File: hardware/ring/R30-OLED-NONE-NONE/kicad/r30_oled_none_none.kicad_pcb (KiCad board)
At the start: 2 copper layers, 43 x 18 mm, 32 parts, among them J1 USB4215-class 16P TH stakes, Q1 SI2301 P-FET, Q2 2N7002 gate driver, SW1 5mm 200gf dome, U1 ESP32-C3-MINI-1-N4, U2 PAW3204DB-TJ3L, U3 TP4054, U4 RT9080-33GJ5

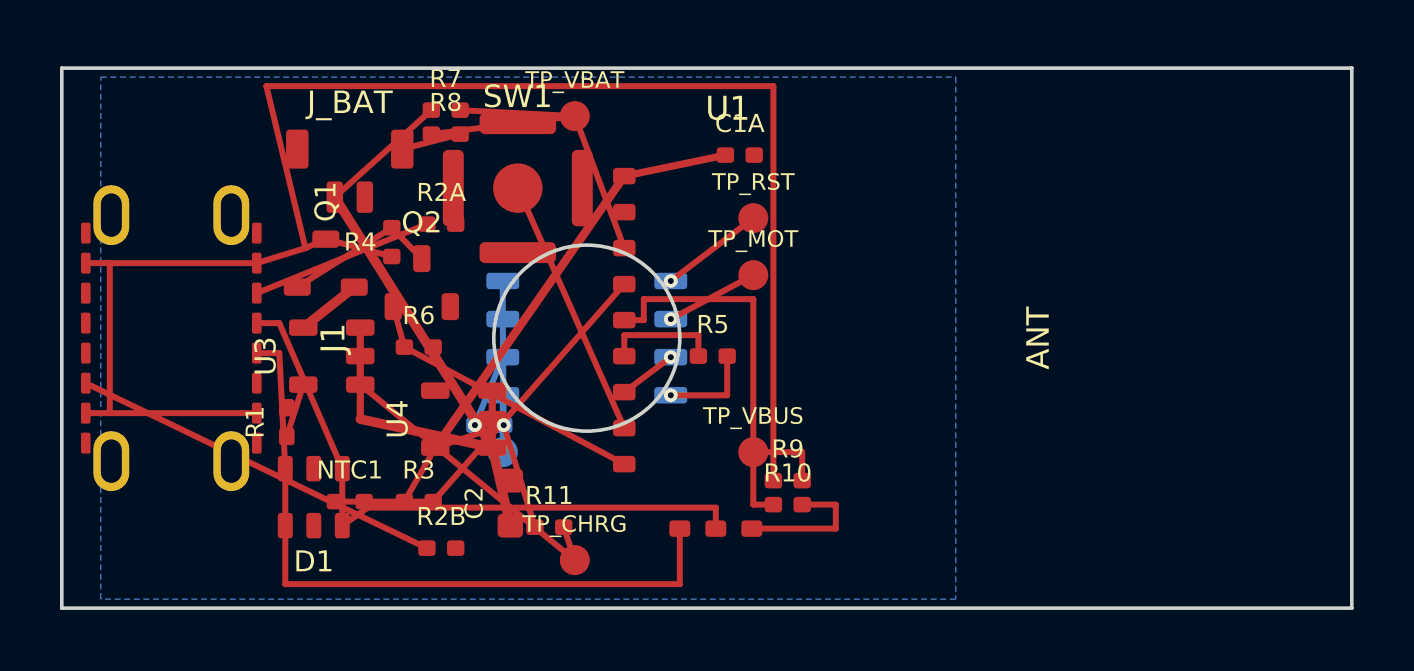
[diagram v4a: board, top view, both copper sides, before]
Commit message: fix(r30): clear connector cluster routing debt
Sensing mechanism: PAW3204 optical surface tracking.

Form factor and angle: R30 30-degree ring, OLED/NONE/NONE active lane; connector-side CC2 and thermistor divider routing cleanup.

Intended use: accessibility-first BLE HID pointing first-board validation.

BOM estimate: active R30 prototype remains about .30-.45, target about ; routing and placement-only change adds no BOM line.
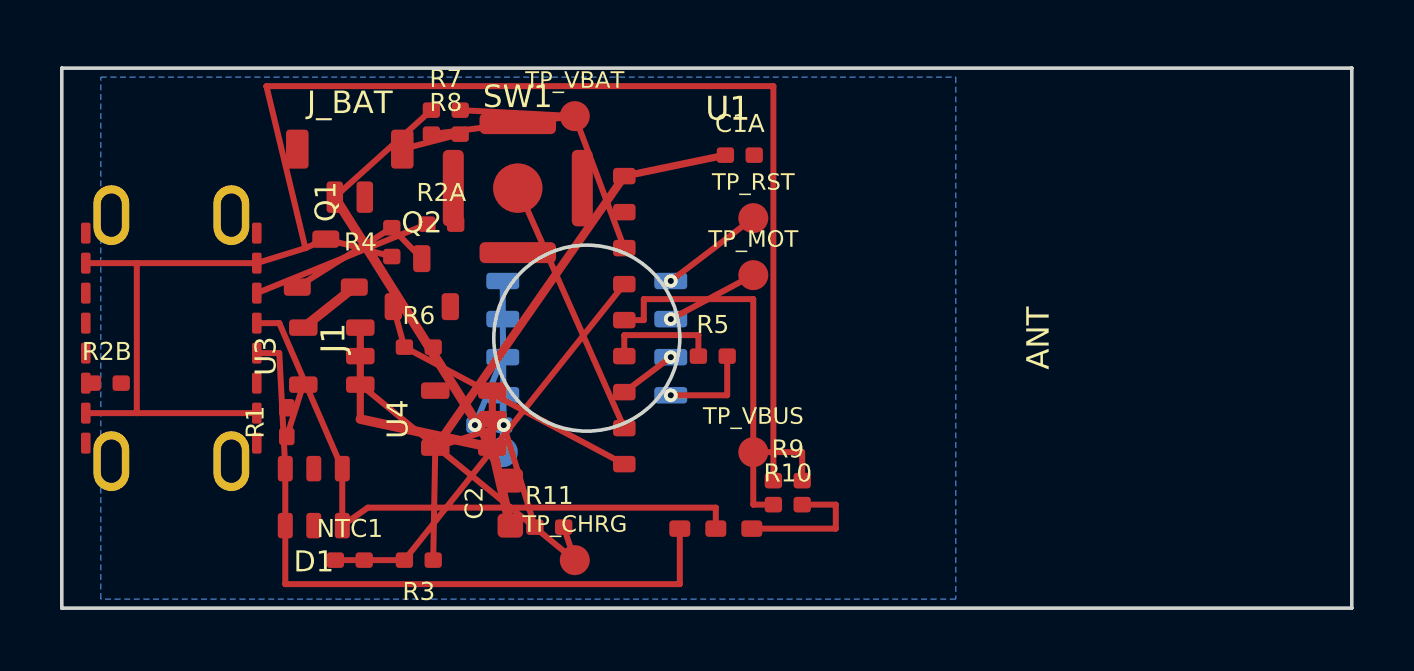
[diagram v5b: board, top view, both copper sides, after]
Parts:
- moved R2B 12.4 mm to (100.5, 101.5)
- moved NTC1 1.95 mm to (108.6, 107.4)
- moved R3 1.95 mm to (110.9, 107.4), turned to 180 degrees
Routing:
- net USB_CC2_RD: track 12.6 -> 0.22 mm
- net VREG_3V3: track 27.3 -> 29.0 mm
- net NTC_SENSE: track 12.9 -> 14.1 mm
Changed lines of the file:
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@@
   (footprint "Resistor_SMD:R_0402_1005Metric"
     (layer "F.Cu")
-    (at 110.900 105.450 0)
+    (at 110.900 107.400 180)
     (property "Reference" "R3" (at 0 -1.05 0) (layer "F.SilkS") (effects (font (size 0.6 0.6) (thickness 0.09))))
     (property "Value" "10k" (at 0 1.05 0) (layer "F.Fab") (effects (font (size 0.55 0.55) (thickness 0.08))))
@@
   (footprint "PowerFinger_Ring:Thermistor_NTC_0402_1005Metric"
     (layer "F.Cu")
-    (at 108.600 105.450 0)
+    (at 108.600 107.400 0)
     (property "Reference" "NTC1" (at 0 -1.05 0) (layer "F.SilkS") (effects (font (size 0.6 0.6) (thickness 0.09))))
     (property "Value" "10k B3950" (at 0 1.05 0) (layer "F.Fab") (effects (font (size 0.55 0.55) (thickness 0.08))))
@@
   (footprint "Resistor_SMD:R_0402_1005Metric"
     (layer "F.Cu")
-    (at 111.650 107.000 0)
+    (at 100.500 101.500 0)
     (property "Reference" "R2B" (at 0 -1.05 0) (layer "F.SilkS") (effects (font (size 0.6 0.6) (thickness 0.09))))
     (property "Value" "5.1k" (at 0 1.05 0) (layer "F.Fab") (effects (font (size 0.55 0.55) (thickness 0.08))))
@@
   (segment (start 105.500 97.500) (end 107.120 97.000) (width 0.20) (layer "F.Cu") (net 2))
   (segment (start 99.800 97.500) (end 105.500 97.500) (width 0.20) (layer "F.Cu") (net 2))
-  (segment (start 99.800 102.500) (end 100.600 102.500) (width 0.20) (layer "F.Cu") (net 2))
-  (segment (start 100.600 102.500) (end 100.600 97.500) (width 0.20) (layer "F.Cu") (net 2))
-  (segment (start 100.600 102.500) (end 105.500 102.500) (width 0.20) (layer "F.Cu") (net 2))
+  (segment (start 99.800 102.500) (end 101.500 102.500) (width 0.20) (layer "F.Cu") (net 2))
+  (segment (start 101.500 102.500) (end 101.500 97.500) (width 0.20) (layer "F.Cu") (net 2))
+  (segment (start 101.500 102.500) (end 105.500 102.500) (width 0.20) (layer "F.Cu") (net 2))
   (segment (start 107.120 97.000) (end 107.800 96.700) (width 0.20) (layer "F.Cu") (net 2))
   (segment (start 107.800 96.700) (end 110.000 97.280) (width 0.20) (layer "F.Cu") (net 2))
@@
   (segment (start 111.450 103.650) (end 117.750 94.600) (width 0.28) (layer "F.Cu") (net 5))
   (segment (start 117.750 94.600) (end 121.120 93.900) (width 0.24) (layer "F.Cu") (net 5))
-  (segment (start 111.450 103.650) (end 110.420 105.450) (width 0.20) (layer "F.Cu") (net 5))
+  (segment (start 111.450 103.650) (end 111.380 107.400) (width 0.20) (layer "F.Cu") (net 5))
   (segment (start 111.450 103.650) (end 113.730 102.900) (width 0.20) (layer "F.Cu") (net 5))
   (segment (start 113.730 102.900) (end 113.700 99.365) (width 0.20) (layer "B.Cu") (net 5))
@@
   (segment (start 114.770 106.300) (end 113.730 102.900) (width 0.20) (layer "F.Cu") (net 5))
   (segment (start 115.730 106.300) (end 116.100 107.400) (width 0.20) (layer "F.Cu") (net 20))
-  (segment (start 108.120 105.450) (end 111.380 105.450) (width 0.20) (layer "F.Cu") (net 9))
-  (segment (start 111.380 105.450) (end 117.750 98.200) (width 0.20) (layer "F.Cu") (net 9))
+  (segment (start 108.120 107.400) (end 110.420 107.400) (width 0.20) (layer "F.Cu") (net 9))
+  (segment (start 110.420 107.400) (end 117.750 98.200) (width 0.20) (layer "F.Cu") (net 9))
   (segment (start 117.750 100.600) (end 117.750 99.900) (width 0.20) (layer "F.Cu") (net 10))
   (segment (start 117.750 99.900) (end 120.220 99.900) (width 0.20) (layer "F.Cu") (net 10))
@@
   (segment (start 119.600 108.200) (end 119.600 106.350) (width 0.20) (layer "F.Cu") (net 17))
   (segment (start 105.500 98.500) (end 111.170 96.200) (width 0.20) (layer "F.Cu") (net 18))
-  (segment (start 99.800 101.500) (end 111.170 107.000) (width 0.20) (layer "F.Cu") (net 19))
+  (segment (start 99.800 101.500) (end 100.020 101.500) (width 0.20) (layer "F.Cu") (net 19))
   (segment (start 108.950 101.550) (end 116.100 107.400) (width 0.20) (layer "F.Cu") (net 20))
   (segment (start 116.100 92.600) (end 117.750 97.000) (width 0.20) (layer "F.Cu") (net 21))

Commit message: fix(r30): reroute usb data escape
Sensing mechanism: PAW3204 optical surface tracking.

Form factor and angle: R30 30-degree ring, OLED/NONE/NONE active lane; A-side USB D+/D- escape moved onto B.Cu under the charger cluster.

Intended use: accessibility-first BLE HID pointing first-board validation.

BOM estimate: active R30 prototype remains about .30-.45, target about ; routing-only change adds no BOM line.
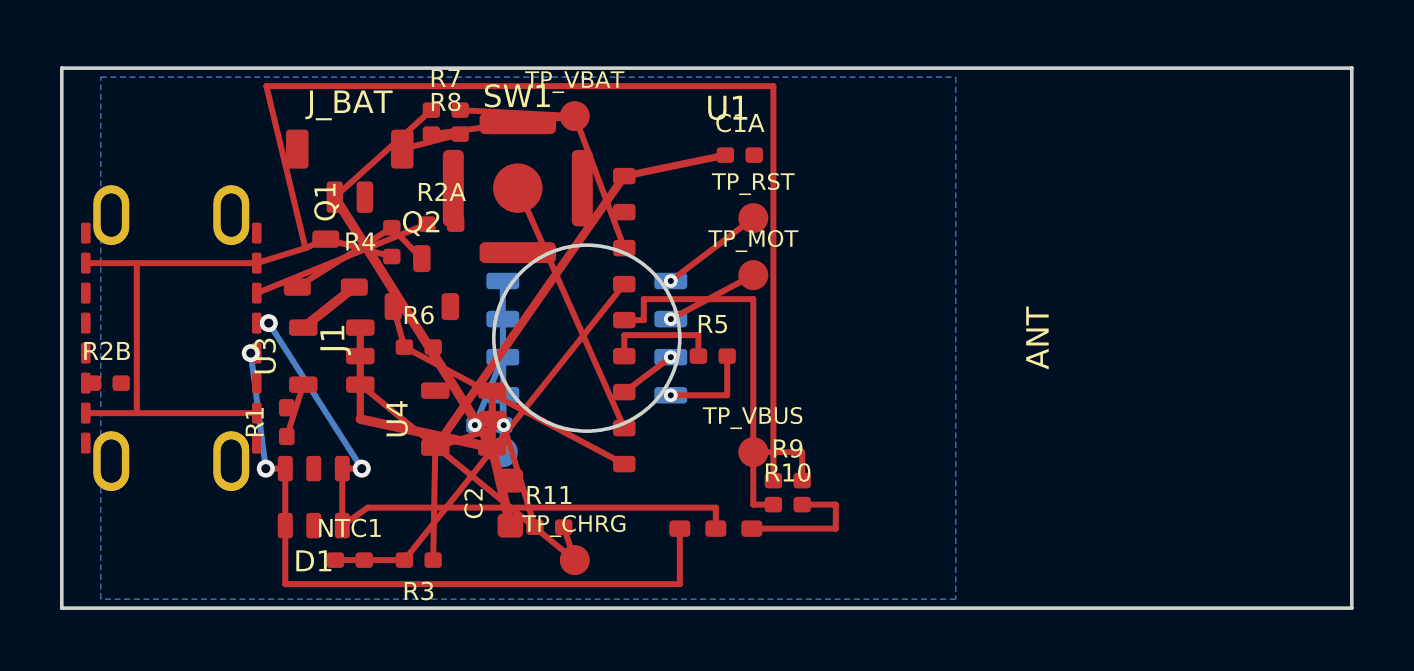
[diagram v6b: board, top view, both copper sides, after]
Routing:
- net USB_D+: track 21.3 -> 22.0 mm, vias 0 -> 2
- net USB_D-: track 23.5 -> 23.6 mm, vias 0 -> 2
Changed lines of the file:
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@@
   (segment (start 119.300 98.095) (end 122.050 96.000) (width 0.20) (layer "F.Cu") (net 14))
   (segment (start 117.750 103.000) (end 114.200 95.000) (width 0.20) (layer "F.Cu") (net 15))
-  (segment (start 105.500 99.500) (end 106.250 99.500) (width 0.20) (layer "F.Cu") (net 16))
-  (segment (start 106.250 99.500) (end 108.350 104.350) (width 0.20) (layer "F.Cu") (net 16))
+  (segment (start 105.500 99.500) (end 105.900 99.500) (width 0.20) (layer "F.Cu") (net 16))
+  (segment (start 105.900 99.500) (end 109.000 104.350) (width 0.20) (layer "B.Cu") (net 16))
+  (segment (start 109.000 104.350) (end 108.350 104.350) (width 0.20) (layer "F.Cu") (net 16))
   (segment (start 108.350 104.350) (end 108.350 106.250) (width 0.20) (layer "F.Cu") (net 16))
   (segment (start 108.350 106.250) (end 109.200 105.650) (width 0.20) (layer "F.Cu") (net 16))
   (segment (start 109.200 105.650) (end 120.800 105.650) (width 0.20) (layer "F.Cu") (net 16))
   (segment (start 120.800 105.650) (end 120.800 106.350) (width 0.20) (layer "F.Cu") (net 16))
-  (segment (start 105.500 100.500) (end 106.250 100.500) (width 0.20) (layer "F.Cu") (net 17))
-  (segment (start 106.250 100.500) (end 106.450 104.350) (width 0.20) (layer "F.Cu") (net 17))
+  (segment (start 105.500 100.500) (end 105.300 100.500) (width 0.20) (layer "F.Cu") (net 17))
+  (segment (start 105.300 100.500) (end 105.800 104.350) (width 0.20) (layer "B.Cu") (net 17))
+  (segment (start 105.800 104.350) (end 106.450 104.350) (width 0.20) (layer "F.Cu") (net 17))
   (segment (start 106.450 104.350) (end 106.450 106.250) (width 0.20) (layer "F.Cu") (net 17))
   (segment (start 106.450 106.250) (end 106.450 108.200) (width 0.20) (layer "F.Cu") (net 17))
@@
   (via (at 119.300 99.365) (size 0.46) (drill 0.20) (layers "F.Cu" "B.Cu") (net 13))
   (via (at 119.300 98.095) (size 0.46) (drill 0.20) (layers "F.Cu" "B.Cu") (net 14))
+  (via (at 105.900 99.500) (size 0.60) (drill 0.30) (layers "F.Cu" "B.Cu") (net 16))
+  (via (at 109.000 104.350) (size 0.60) (drill 0.30) (layers "F.Cu" "B.Cu") (net 16))
+  (via (at 105.300 100.500) (size 0.60) (drill 0.30) (layers "F.Cu" "B.Cu") (net 17))
+  (via (at 105.800 104.350) (size 0.60) (drill 0.30) (layers "F.Cu" "B.Cu") (net 17))
 )

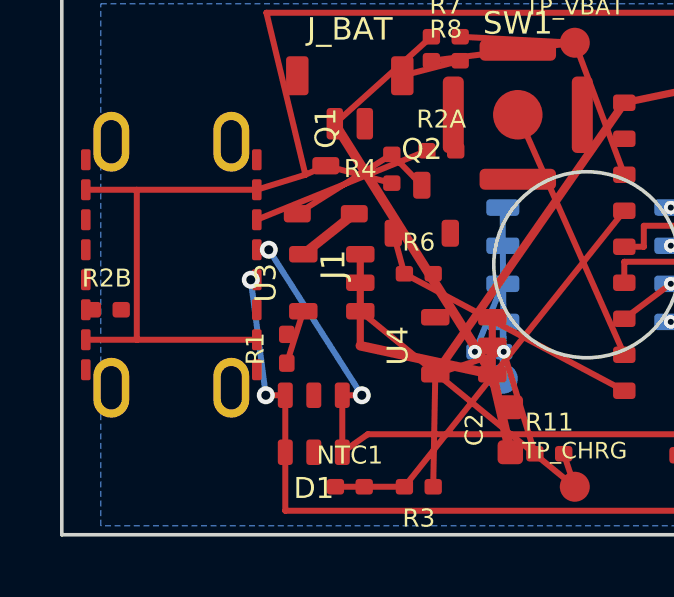
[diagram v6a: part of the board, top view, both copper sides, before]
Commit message: fix(r30): connect mirrored usb data pads
Sensing mechanism: PAW3204 optical surface tracking.

Form factor and angle: R30 30-degree ring, OLED/NONE/NONE active lane; mirrored USB-C B6/B7 data pads routed into the existing data escape.

Intended use: accessibility-first BLE HID pointing first-board validation.

BOM estimate: active R30 prototype remains about .30-.45, target about ; routing-only change adds no BOM line.
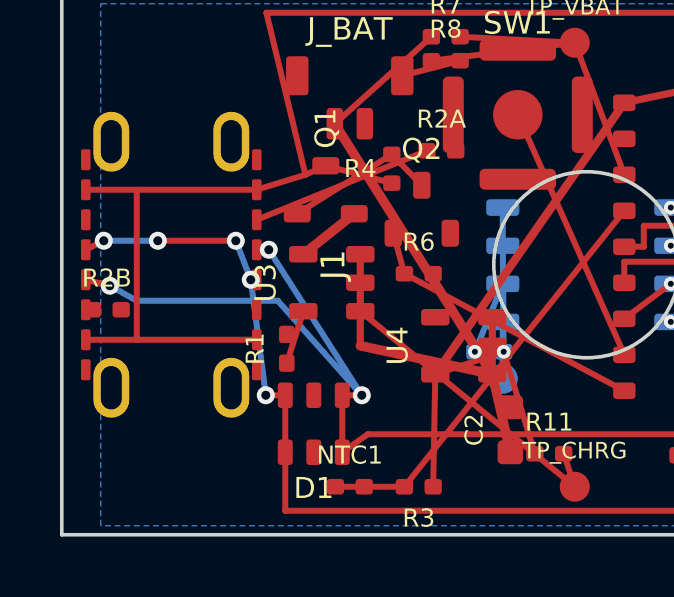
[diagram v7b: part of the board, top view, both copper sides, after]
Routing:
- net USB_D+: track 22.0 -> 32.8 mm, vias 2 -> 3
- net USB_D-: track 23.6 -> 30.0 mm, vias 2 -> 5
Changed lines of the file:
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@@
   (segment (start 119.300 98.095) (end 122.050 96.000) (width 0.20) (layer "F.Cu") (net 14))
   (segment (start 117.750 103.000) (end 114.200 95.000) (width 0.20) (layer "F.Cu") (net 15))
+  (segment (start 99.800 100.500) (end 100.600 100.700) (width 0.20) (layer "F.Cu") (net 16))
+  (segment (start 100.600 100.700) (end 101.500 101.200) (width 0.20) (layer "B.Cu") (net 16))
+  (segment (start 101.500 101.200) (end 106.200 101.200) (width 0.20) (layer "B.Cu") (net 16))
+  (segment (start 106.200 101.200) (end 109.000 104.350) (width 0.20) (layer "B.Cu") (net 16))
   (segment (start 105.500 99.500) (end 105.900 99.500) (width 0.20) (layer "F.Cu") (net 16))
   (segment (start 105.900 99.500) (end 109.000 104.350) (width 0.20) (layer "B.Cu") (net 16))
@@
   (segment (start 109.200 105.650) (end 120.800 105.650) (width 0.20) (layer "F.Cu") (net 16))
   (segment (start 120.800 105.650) (end 120.800 106.350) (width 0.20) (layer "F.Cu") (net 16))
+  (segment (start 99.800 99.500) (end 100.400 99.200) (width 0.20) (layer "F.Cu") (net 17))
+  (segment (start 100.400 99.200) (end 102.200 99.200) (width 0.20) (layer "B.Cu") (net 17))
+  (segment (start 102.200 99.200) (end 104.800 99.200) (width 0.20) (layer "F.Cu") (net 17))
+  (segment (start 104.800 99.200) (end 105.300 100.500) (width 0.20) (layer "B.Cu") (net 17))
   (segment (start 105.500 100.500) (end 105.300 100.500) (width 0.20) (layer "F.Cu") (net 17))
   (segment (start 105.300 100.500) (end 105.800 104.350) (width 0.20) (layer "B.Cu") (net 17))
@@
   (via (at 105.300 100.500) (size 0.60) (drill 0.30) (layers "F.Cu" "B.Cu") (net 17))
   (via (at 105.800 104.350) (size 0.60) (drill 0.30) (layers "F.Cu" "B.Cu") (net 17))
+  (via (at 100.600 100.700) (size 0.60) (drill 0.30) (layers "F.Cu" "B.Cu") (net 16))
+  (via (at 100.400 99.200) (size 0.60) (drill 0.30) (layers "F.Cu" "B.Cu") (net 17))
+  (via (at 102.200 99.200) (size 0.60) (drill 0.30) (layers "F.Cu" "B.Cu") (net 17))
+  (via (at 104.800 99.200) (size 0.60) (drill 0.30) (layers "F.Cu" "B.Cu") (net 17))
 )
